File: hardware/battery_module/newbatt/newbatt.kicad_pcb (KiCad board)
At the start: 2 copper layers, 66.5 x 60.5 mm, 17 parts, among them J1 Barrel_Jack_MountingPin, J2 USB_C_Receptacle_PowerOnly_24P, J3 USB_B_Micro, J4 Screw_Terminal_01x02, J5 Screw_Terminal_01x02, U1 BQ25172DSGR

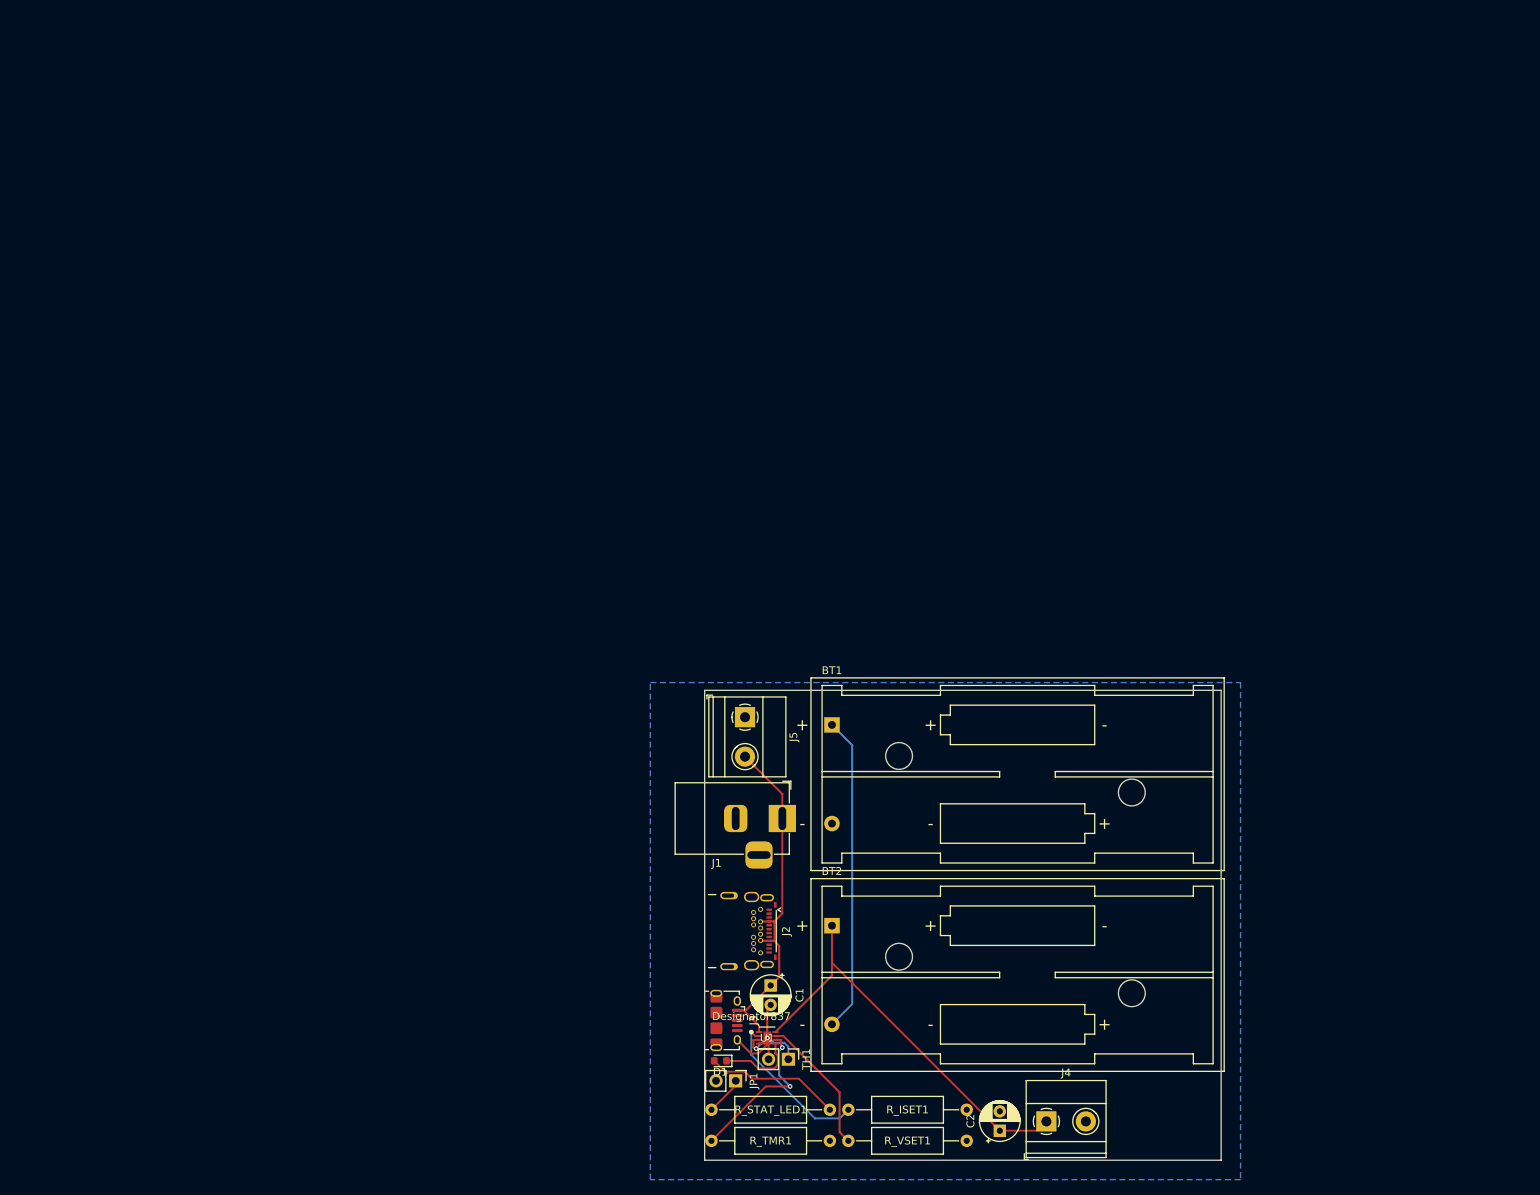
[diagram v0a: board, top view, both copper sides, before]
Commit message: BQ25756E NiMH solar charging
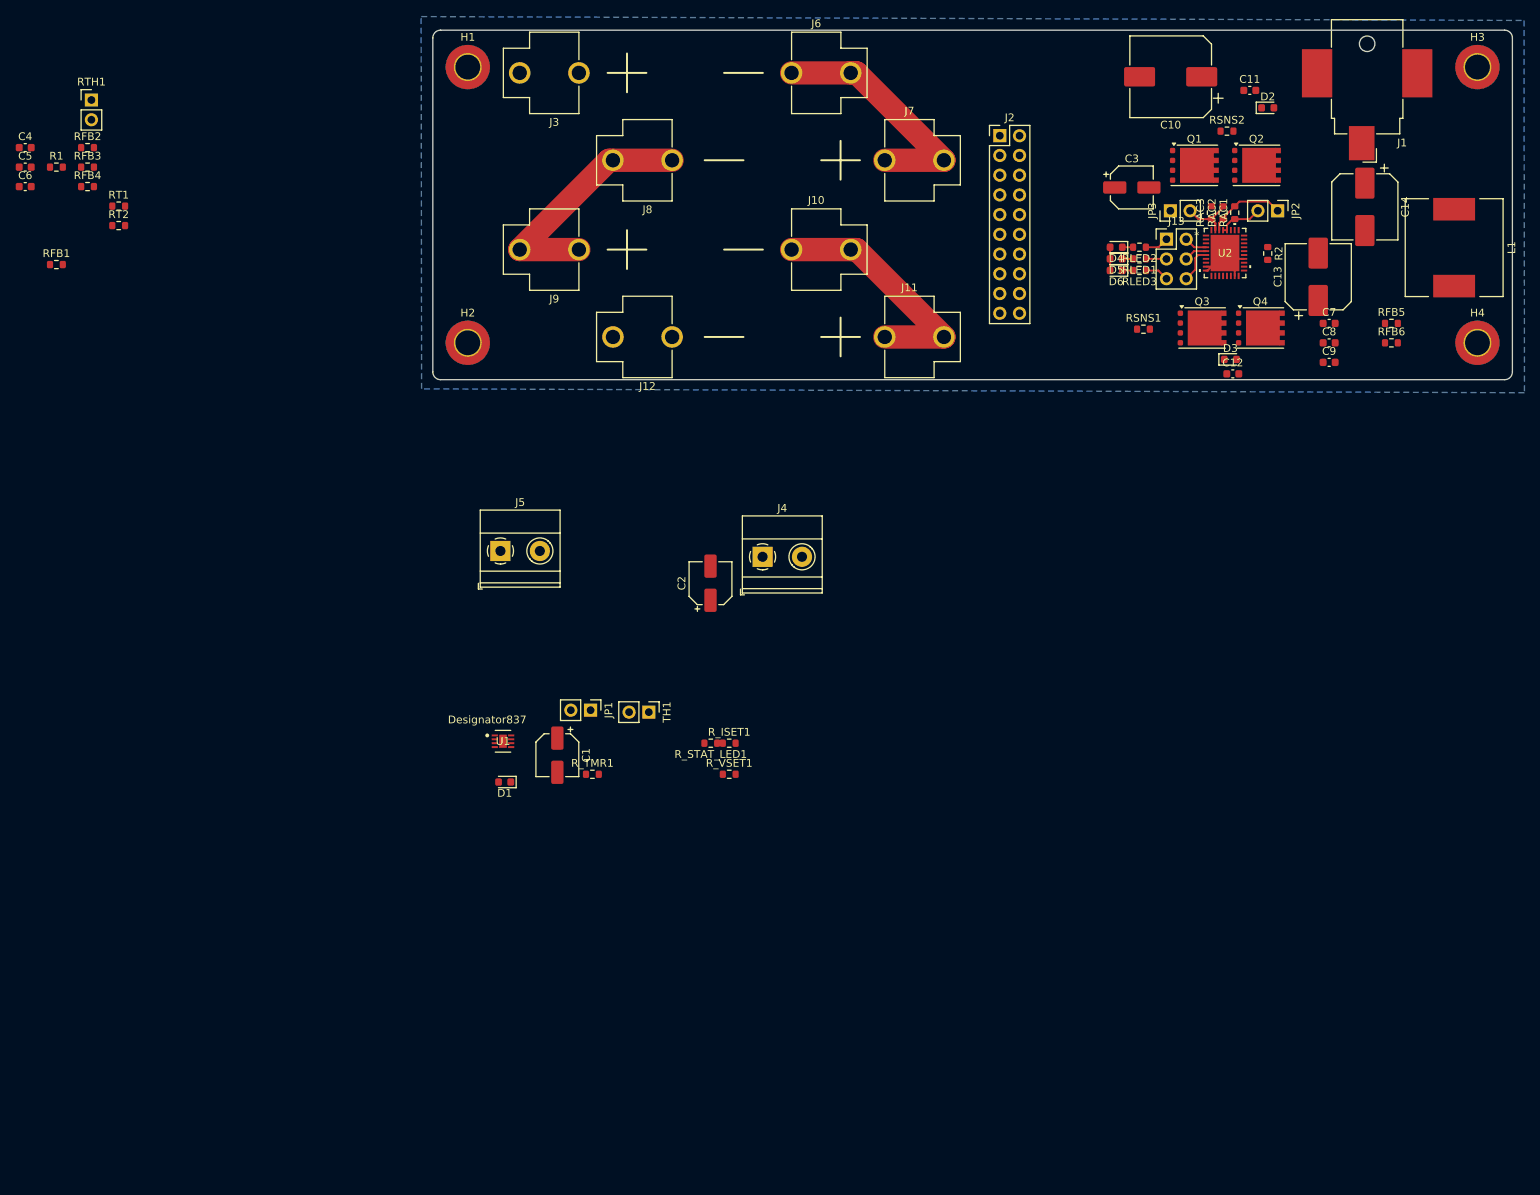
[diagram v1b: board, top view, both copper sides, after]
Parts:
- removed BT1, BT2: ~, Battery:BatteryHolder_Keystone_2468_2xAAA
- added C10: 80 uF, Capacitor_SMD:CP_Elec_10x10, F.Cu at (110.0, 21.0)
- added C11: 100 nF, Capacitor_SMD:C_0603_1608Metric, F.Cu at (120.2, 22.8)
- added C12: 100 nF, Capacitor_SMD:C_0603_1608Metric, F.Cu at (118.0, 59.2)
- added C13: 4.7 uF, Capacitor_SMD:CP_Elec_8x5.4, F.Cu at (129.0, 46.8)
- added C14: 4.7 uF, Capacitor_SMD:CP_Elec_8x5.4, F.Cu at (135.0, 37.8)
- added C3: 1 uF, Capacitor_SMD:CP_Elec_5x3, F.Cu at (105.0, 35.2)
- added C4: 470 nF, Capacitor_SMD:C_0603_1608Metric, F.Cu at (-37.5, 30.1)
- added C5: 100 nF, Capacitor_SMD:C_0603_1608Metric, F.Cu at (-37.5, 32.6)
- added C6: 100 nF, Capacitor_SMD:C_0603_1608Metric, F.Cu at (-37.5, 35.1)
- added C7: 470 nF, Capacitor_SMD:C_0603_1608Metric, F.Cu at (130.4, 52.8)
- added C8: 100 nF, Capacitor_SMD:C_0603_1608Metric, F.Cu at (130.4, 55.3)
- added C9: 100 nF, Capacitor_SMD:C_0603_1608Metric, F.Cu at (130.4, 57.8)
- added D2: D_Small_Filled, Diode_SMD:D_0603_1608Metric, F.Cu at (122.5, 25.0)
- added D3: D_Small_Filled, Diode_SMD:D_0603_1608Metric, F.Cu at (117.7, 57.4)
- added D4: LED, LED_SMD:LED_0603_1608Metric, F.Cu at (103.0, 42.9)
- added D5: LED, LED_SMD:LED_0603_1608Metric, F.Cu at (103.0, 44.4)
- added D6: LED, LED_SMD:LED_0603_1608Metric, F.Cu at (103.0, 45.9)
- added H1: MountingHole_Pad, MountingHole:MountingHole_3.2mm_M3_ISO7380_Pad_TopBottom, F.Cu at (19.5, 19.8)
- added H2: MountingHole_Pad, MountingHole:MountingHole_3.2mm_M3_ISO7380_Pad_TopBottom, F.Cu at (19.5, 55.2)
- added H3: MountingHole_Pad, MountingHole:MountingHole_3.2mm_M3_ISO7380_Pad_TopBottom, F.Cu at (149.5, 19.8)
- added H4: MountingHole_Pad, MountingHole:MountingHole_3.2mm_M3_ISO7380_Pad_TopBottom, F.Cu at (149.5, 55.2)
- added J10: Conn_01x01_Socket, Keystone82:BAT_82, F.Cu at (65.0, 43.2)
- added J11: Conn_01x01_Socket, Keystone82:BAT_82, F.Cu at (77.0, 54.5)
- added J12: Conn_01x01_Socket, Keystone82:BAT_82, F.Cu at (42.0, 54.5)
- added J13: Conn_02x03_Odd_Even, Connector_PinHeader_2.54mm:PinHeader_2x03_P2.54mm_Vertical, F.Cu at (109.5, 41.9)
- added J6: Conn_01x01_Socket, Keystone82:BAT_82, F.Cu at (65.0, 20.5)
- added J7: Conn_01x01_Socket, Keystone82:BAT_82, F.Cu at (77.0, 31.8)
- added J8: Conn_01x01_Socket, Keystone82:BAT_82, F.Cu at (42.0, 31.8)
- added J9: Conn_01x01_Socket, Keystone82:BAT_82, F.Cu at (30.0, 43.2)
- added JP2: Jumper_2_Small_Open, Connector_PinHeader_2.54mm:PinHeader_1x02_P2.54mm_Vertical, F.Cu at (123.8, 38.2)
- added JP3: Jumper_2_Small_Open, Connector_PinHeader_2.54mm:PinHeader_1x02_P2.54mm_Vertical, F.Cu at (110.0, 38.2)
- added L1: 10 uH, Inductor_SMD:L_12x12mm_H8mm, F.Cu at (146.5, 43.0)
- added Q1: NMOS, Package_SON:VSONP-8-1EP_5x6_P1.27mm, F.Cu at (113.0, 32.4)
- added Q2: NMOS, Package_SON:VSONP-8-1EP_5x6_P1.27mm, F.Cu at (121.0, 32.4)
- added Q3: NMOS, Package_SON:VSONP-8-1EP_5x6_P1.27mm, F.Cu at (114.0, 53.3)
- added Q4: NMOS, Package_SON:VSONP-8-1EP_5x6_P1.27mm, F.Cu at (121.5, 53.3)
- added R1: 133 kOhm, Resistor_SMD:R_0603_1608Metric, F.Cu at (-33.5, 32.6)
- added R2: 10 Ohm, Resistor_SMD:R_0603_1608Metric, F.Cu at (122.5, 43.8)
- added RAC1: R_Small_US, Resistor_SMD:R_0603_1608Metric, F.Cu at (118.2, 38.5)
- added RAC2: R_Small_US, Resistor_SMD:R_0603_1608Metric, F.Cu at (116.8, 38.5)
- added RAC3: R_Small_US, Resistor_SMD:R_0603_1608Metric, F.Cu at (115.2, 38.5)
- added RFB1: 249 kOhm, Resistor_SMD:R_0603_1608Metric, F.Cu at (-33.5, 45.2)
- added RFB2: 24.88 kOhm, Resistor_SMD:R_0603_1608Metric, F.Cu at (-29.5, 30.1)
- added RFB3: 10 Ohm, Resistor_SMD:R_0603_1608Metric, F.Cu at (-29.5, 32.6)
- added RFB4: 10 Ohm, Resistor_SMD:R_0603_1608Metric, F.Cu at (-29.5, 35.1)
- added RFB5: 10 Ohm, Resistor_SMD:R_0603_1608Metric, F.Cu at (138.4, 52.8)
- added RFB6: 10 Ohm, Resistor_SMD:R_0603_1608Metric, F.Cu at (138.4, 55.3)
- added RLED1: 300 Ohm, Resistor_SMD:R_0603_1608Metric, F.Cu at (106.0, 44.4)
- added RLED2: 300 Ohm, Resistor_SMD:R_0603_1608Metric, F.Cu at (106.0, 42.9)
- added RLED3: 300 Ohm, Resistor_SMD:R_0603_1608Metric, F.Cu at (106.0, 45.9)
- added RSNS1: 5 mOhm, Resistor_SMD:R_0603_1608Metric, F.Cu at (106.5, 53.5)
- added RSNS2: 5 mOhm, Resistor_SMD:R_0603_1608Metric, F.Cu at (117.2, 28.0)
- added RT1: 5.24 kOhm, Resistor_SMD:R_0603_1608Metric, F.Cu at (-25.4, 37.6)
- added RT2: 30.31 kOhm, Resistor_SMD:R_0603_1608Metric, F.Cu at (-25.4, 40.2)
- added RTH1: 10 kOhm NTC, Connector_PinHeader_2.54mm:PinHeader_1x02_P2.54mm_Vertical, F.Cu at (-29.0, 24.0)
- added U2: BQ25756ERRVR, BQ25756E:VQFN36_RRV_TEX, F.Cu at (117.0, 43.7)
- C1, C2: footprint Capacitor_THT:CP_Radial_D5.0mm_P2.50mm -> Capacitor_SMD:CP_Elec_5x3
- J1: footprint Connector_BarrelJack:BarrelJack_Horizontal -> Connector_BarrelJack:BarrelJack_CUI_PJ-036AH-SMT_Horizontal
- J2: value USB_C_Receptacle_PowerOnly_24P -> Conn_02x10_Odd_Even; footprint Connector_USB:USB_C_Receptacle_CNCTech_C-ARA1-AK51X -> Connector_PinHeader_2.54mm:PinHeader_2x10_P2.54mm_Vertical
- J3: value USB_B_Micro -> Conn_01x01_Socket; footprint Connector_USB:USB_Micro-B_Amphenol_10118194_Horizontal -> Keystone82:BAT_82
- R_ISET1, R_STAT_LED1, R_TMR1, R_VSET1: footprint Resistor_THT:R_Axial_DIN0309_L9.0mm_D3.2mm_P15.24mm_Horizontal -> Resistor_SMD:R_0603_1608Metric
- moved J3 124.1 mm to (30.0, 20.5), turned to 180 degrees
- moved J1 119.5 mm to (135.3, 23.8), turned to 180 degrees
- moved J2 107.6 mm to (88.0, 28.6), turned to 0 degrees
- moved J4 81.4 mm to (57.5, 82.8)
- moved C2 79.7 mm to (50.8, 86.2)
- moved JP1 51.3 mm to (35.3, 102.6)
- moved U1 51.1 mm to (24.0, 106.6)
- moved R_ISET1 49.6 mm to (53.2, 106.8)
- moved R_STAT_LED1 49.6 mm to (50.8, 106.8)
- moved R_TMR1 49.6 mm to (35.5, 110.8)
- moved R_VSET1 49.6 mm to (53.2, 110.8)
- moved TH1 48.2 mm to (42.8, 102.8)
- moved D1 45.4 mm to (24.2, 111.8)
- moved C1 40.4 mm to (31.0, 108.3)
- moved J5 38.1 mm to (23.7, 82.1), turned to 0 degrees
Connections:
- J1 pad 1: /VIN -> VSOURCE
- J3 pad 1: /VIN -> VBAT
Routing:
- net /VOUT: track 58.6 -> 0.00 mm
- net Net-(BT1-+): track 40.7 -> 0.00 mm
- net /VIN: track 46.3 -> 5.92 mm
- net Net-(J8-Pin_1): track 0.00 -> 32.0 mm
- net Net-(J6-Pin_1): track 0.00 -> 31.9 mm
- net Net-(J10-Pin_1): track 0.00 -> 31.9 mm
- net Net-(U1-TMR): track 20.5 -> 0.00 mm, vias 2 -> 0
- net Net-(U1-ISET): track 20.5 -> 0.00 mm, vias 1 -> 0
- net Net-(U1-VSET): track 18.0 -> 0.00 mm
- net Net-(D1-A): track 17.8 -> 0.00 mm
- net Net-(JP2-A): track 0.00 -> 10.2 mm
- net Net-(D1-K): track 10.0 -> 0.00 mm
- net Net-(U1-TS): track 8.36 -> 0.00 mm, vias 1 -> 0
- net Net-(JP3-B): track 0.00 -> 8.00 mm
- net Net-(JP1-A): track 5.02 -> 0.00 mm
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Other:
- board size 66.5 x 60.5 mm -> 139 x 45 mm

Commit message: 18650 Li-Ion 2 parallel design using BQ24210
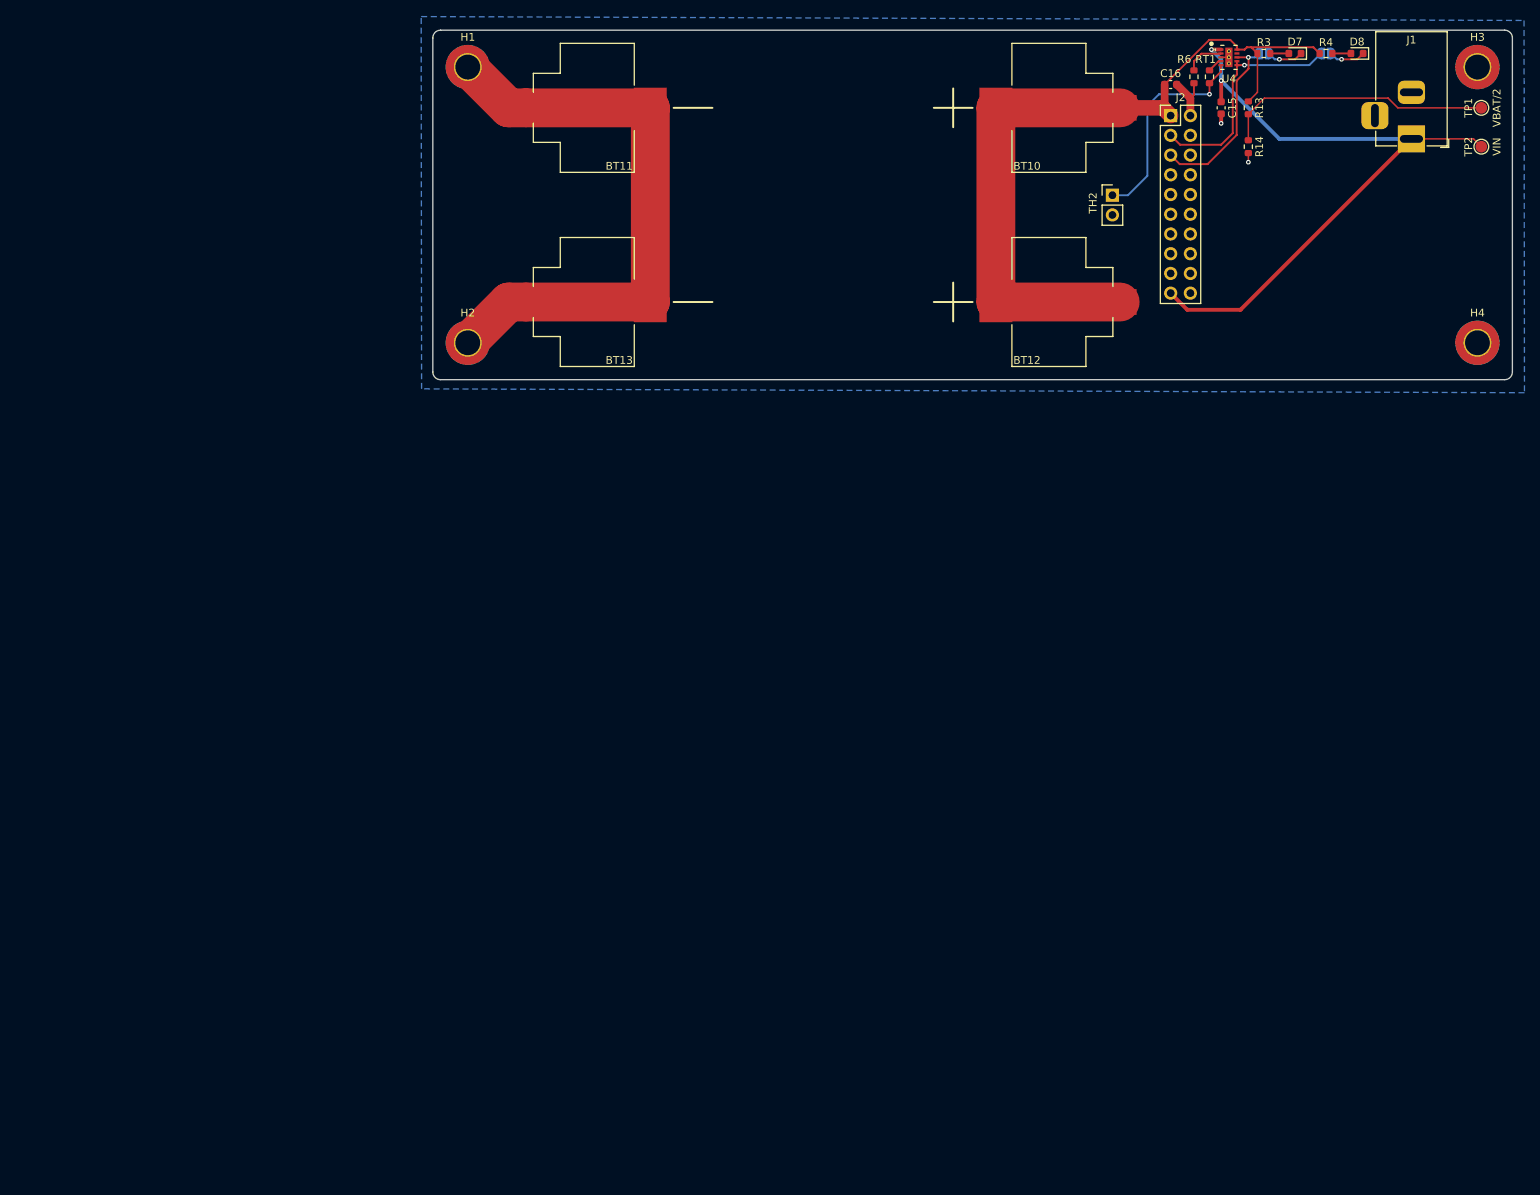
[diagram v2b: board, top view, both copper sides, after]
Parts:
- removed C1, C2, C3: 1 uF, Capacitor_SMD:CP_Elec_5x3
- removed C10: 80 uF, Capacitor_SMD:CP_Elec_10x10
- removed C11, C12, C5, C6, C8, C9: 100 nF, Capacitor_SMD:C_0603_1608Metric
- removed C13, C14: 4.7 uF, Capacitor_SMD:CP_Elec_8x5.4
- removed C4, C7: 470 nF, Capacitor_SMD:C_0603_1608Metric
- removed D1, D4, D5, D6: LED, LED_SMD:LED_0603_1608Metric
- removed D2, D3: D_Small_Filled, Diode_SMD:D_0603_1608Metric
- removed J10, J11, J12, J3, J6, J7, J8, J9: Conn_01x01_Socket, Keystone82:BAT_82
- removed J13: Conn_02x03_Odd_Even, Connector_PinHeader_2.54mm:PinHeader_2x03_P2.54mm_Vertical
- removed J4, J5: Screw_Terminal_01x02, TerminalBlock_Phoenix:TerminalBlock_Phoenix_MKDS-1,5-2-5.08_1x02_P5.08mm_Horizontal
- removed JP1: Jumper_2_Bridged, Connector_PinHeader_2.54mm:PinHeader_1x02_P2.54mm_Vertical
- removed JP2, JP3: Jumper_2_Small_Open, Connector_PinHeader_2.54mm:PinHeader_1x02_P2.54mm_Vertical
- removed L1: 10 uH, Inductor_SMD:L_12x12mm_H8mm
- removed Q1, Q2, Q3, Q4: NMOS, Package_SON:VSONP-8-1EP_5x6_P1.27mm
- removed R1: 133 kOhm, Resistor_SMD:R_0603_1608Metric
- removed R2, RFB3, RFB4, RFB5, RFB6: 10 Ohm, Resistor_SMD:R_0603_1608Metric
- removed RAC1, RAC2, RAC3: R_Small_US, Resistor_SMD:R_0603_1608Metric
- removed RFB1: 249 kOhm, Resistor_SMD:R_0603_1608Metric
- removed RFB2: 24.88 kOhm, Resistor_SMD:R_0603_1608Metric
- removed RLED1, RLED2, RLED3, R_STAT_LED1: 300 Ohm, Resistor_SMD:R_0603_1608Metric
- removed RSNS1, RSNS2: 5 mOhm, Resistor_SMD:R_0603_1608Metric
- removed RT2: 30.31 kOhm, Resistor_SMD:R_0603_1608Metric
- removed RTH1, TH1: 10 kOhm NTC, Connector_PinHeader_2.54mm:PinHeader_1x02_P2.54mm_Vertical
- removed R_ISET1: 375 Ohm, Resistor_SMD:R_0603_1608Metric
- removed R_TMR1: 15 kOhm, Resistor_SMD:R_0603_1608Metric
- removed R_VSET1: 11 kOhm, Resistor_SMD:R_0603_1608Metric
- removed U1: BQ25172DSGR, BQ25172:DSG0008A-IPC_A
- removed U2: BQ25756ERRVR, BQ25756E:VQFN36_RRV_TEX
- added BT10: 254TR, Keystone254TR:BAT_254TR, F.Cu at (95.5, 25.0)
- added BT11: 254TR, Keystone254TR:BAT_254TR, F.Cu at (35.0, 25.0)
- added BT12: 254TR, Keystone254TR:BAT_254TR, F.Cu at (95.5, 50.0)
- added BT13: 254TR, Keystone254TR:BAT_254TR, F.Cu at (35.0, 50.0)
- added C15: 1 uF, Capacitor_SMD:C_0603_1608Metric, F.Cu at (116.5, 25.0)
- added C16: 1 uF, Capacitor_SMD:C_0603_1608Metric, F.Cu at (110.0, 22.0)
- added D7: LED, LED_SMD:LED_0603_1608Metric, F.Cu at (126.0, 18.0)
- added D8: LED, LED_SMD:LED_0603_1608Metric, F.Cu at (134.0, 18.0)
- added JP4: Jumper_2_Small_Open, Jumper:SolderJumper-2_P1.3mm_Open_RoundedPad1.0x1.5mm, B.Cu at (122.0, 18.0)
- added JP5: Jumper_2_Small_Open, Jumper:SolderJumper-2_P1.3mm_Open_RoundedPad1.0x1.5mm, B.Cu at (130.0, 18.0)
- added R13: 1 MOhm, Resistor_SMD:R_0603_1608Metric, F.Cu at (120.0, 25.0)
- added R14: 1 MOhm, Resistor_SMD:R_0603_1608Metric, F.Cu at (120.0, 30.0)
- added R3: 2 kOhm, Resistor_SMD:R_0603_1608Metric, F.Cu at (122.0, 18.0)
- added R4: 2 kOhm, Resistor_SMD:R_0603_1608Metric, F.Cu at (130.0, 18.0)
- added R6: R_Small_US, Resistor_SMD:R_0603_1608Metric, F.Cu at (113.0, 21.0)
- added TH2: 103AT NTC, Connector_PinHeader_2.54mm:PinHeader_1x02_P2.54mm_Vertical, F.Cu at (102.5, 36.2)
- added TP1: VBAT sense, TestPoint:TestPoint_Pad_D1.5mm, F.Cu at (150.0, 25.0)
- added TP2: Vin, TestPoint:TestPoint_Pad_D1.5mm, F.Cu at (150.0, 30.0)
- added U4: BQ24210DQCR, BQ24210:DQC10_P84X2P4, F.Cu at (117.5, 18.5)
- J1: footprint Connector_BarrelJack:BarrelJack_CUI_PJ-036AH-SMT_Horizontal -> Connector_BarrelJack:BarrelJack_Horizontal
- RT1: value 5.24 kOhm -> R_Small_US
- moved RT1 141.4 mm to (115.0, 21.0), turned to -90 degrees
- moved J2 22.2 mm to (110.0, 26.0)
- moved J1 7.75 mm to (141.0, 29.0), turned to -90 degrees
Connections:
- J1 pad 1: VSOURCE -> VIN
- J1 pad 3: unconnected-(J1-MountPin-Pad3) -> (no net)
- J2 pad 1: SCL -> VOUT
- J2 pad 11: /STAT2 -> unconnected-(J2-Pin_11-Pad11)
- J2 pad 13: /PG -> unconnected-(J2-Pin_13-Pad13)
- J2 pad 15: TS -> unconnected-(J2-Pin_15-Pad15)
- J2 pad 17: VSOURCE -> unconnected-(J2-Pin_17-Pad17)
- J2 pad 19: VBAT -> VIN
- J2 pad 3: SDA -> /~{PG}
- J2 pad 5: INT -> /~{CHG}
- J2 pad 7: CE -> unconnected-(J2-Pin_7-Pad7)
- J2 pad 9: /STAT1 -> unconnected-(J2-Pin_9-Pad9)
- RT1 pad 1: /REGN -> Net-(U4-VTSB)
- RT1 pad 2: TS -> Net-(U4-TS)
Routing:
- net VOUT: track 0.00 -> 99.6 mm
- net VIN: track 0.00 -> 86.5 mm, vias 0 -> 2
- net 0: track 12.8 -> 86.6 mm, vias 0 -> 2
- net Net-(R13-Pad2): track 0.00 -> 34.7 mm
- net Net-(J8-Pin_1): track 32.0 -> 0.00 mm
- net Net-(J6-Pin_1): track 31.9 -> 0.00 mm
- net Net-(J10-Pin_1): track 31.9 -> 0.00 mm
- net /~{PG}: track 0.00 -> 30.0 mm, vias 0 -> 1
- net Net-(U4-TS): track 0.00 -> 27.5 mm, vias 0 -> 1
- net /~{CHG}: track 0.00 -> 24.2 mm, vias 0 -> 1
- net Net-(JP2-A): track 10.2 -> 0.00 mm
- net Net-(JP3-B): track 8.00 -> 0.00 mm
- net /VIN: track 5.92 -> 0.00 mm
- net Net-(U4-ISET): track 0.00 -> 5.06 mm
- net Net-(D8-K): track 0.00 -> 4.76 mm, vias 0 -> 1
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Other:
- board text added: "VBAT/2"
- board text added: "VIN"
